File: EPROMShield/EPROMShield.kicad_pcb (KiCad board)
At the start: 2 copper layers, 101.6 x 53.3 mm, 79 parts, among them J1 Conn_02x16_Counter_Clockwise, P1 Digital, P10 CONN_01X01, P11 CONN_01X01, P12 CONN_01X01, P13 CONN_01X01, P2 Power, P3 Analog, P4 Analog, P5 PWM, P6 PWM, P7 Communication, P8 CONN_01X01, P9 CONN_01X01, Q1 BC847, Q2 BC847, Q3 BSS83P, Q4 BSS83P, Q5 BSS83P, Q6 BSS138, Q7 BC847, Q8 BC847, U1 MC34063AD, U2 LM317_TO-220, U3 74AHC1GU04

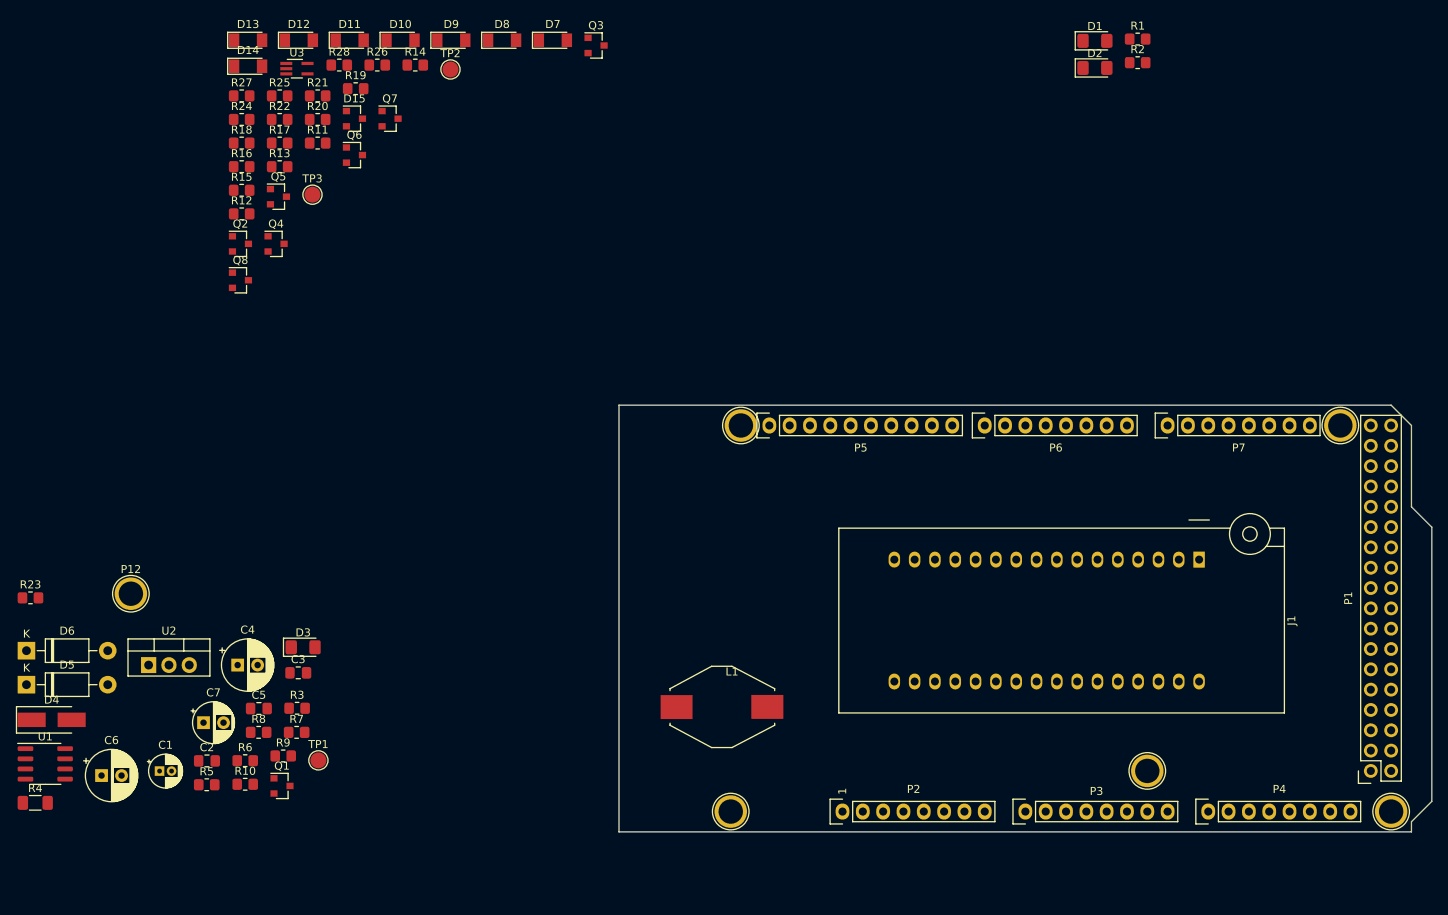
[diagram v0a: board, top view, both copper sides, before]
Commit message: First shot at component placement. Fixed VCC connection for Inverter
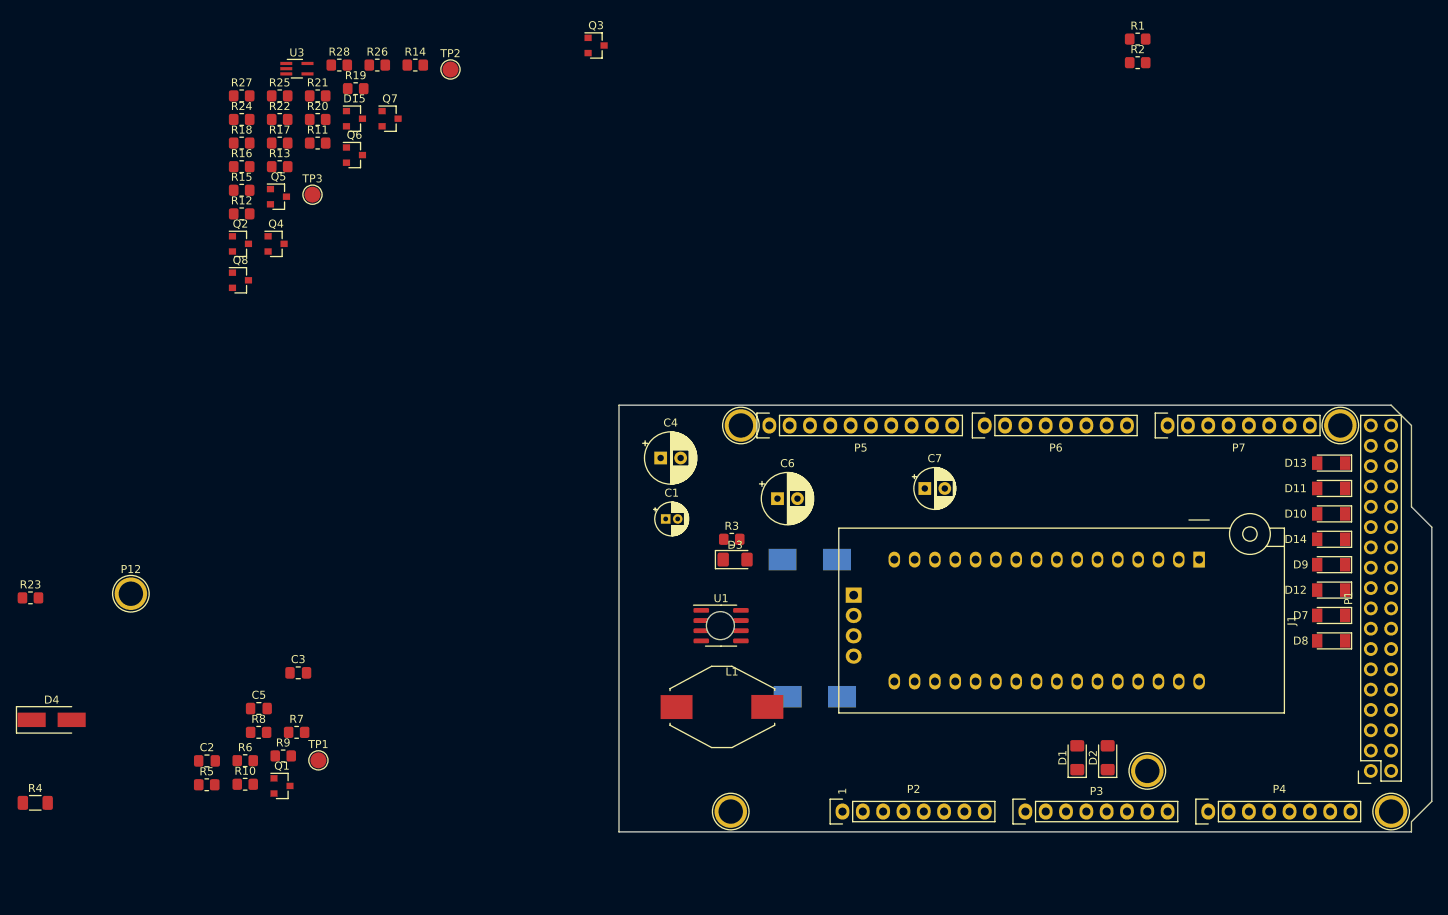
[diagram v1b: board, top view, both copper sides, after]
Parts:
- D5, D6: footprint Diode_THT:D_DO-41_SOD81_P10.16mm_Horizontal -> Diode_SMD:D_MELF_Handsoldering; moved to B.Cu
- U2: footprint Package_TO_SOT_THT:TO-220-3_Vertical -> Package_TO_SOT_THT:TO-220-4_Horizontal_TabDown; moved to B.Cu
- moved D14 147.7 mm to (192.4, 85.1), turned to 180 degrees
- moved D12 146.2 mm to (192.4, 91.4), turned to 180 degrees
- moved D13 145.3 mm to (192.4, 75.6), turned to 180 degrees
- moved D11 134.9 mm to (192.4, 78.7), turned to 180 degrees
- moved D10 130.5 mm to (192.4, 81.9), turned to 180 degrees
- moved D9 128.0 mm to (192.4, 88.3), turned to 180 degrees
- moved D8 128.0 mm to (192.4, 97.8), turned to 180 degrees
- moved D7 121.0 mm to (192.4, 94.6), turned to 180 degrees
- moved D6 98.6 mm to (127.2, 87.6)
- moved D5 98.6 mm to (127.9, 104.8)
- moved C7 94.8 mm to (141.6, 78.7)
- moved C6 91.3 mm to (123.2, 80.0)
- moved D1 89.6 mm to (160.7, 112.4), turned to 90 degrees
- moved U2 88.6 mm to (132.7, 92.1), turned to 270 degrees
- moved D2 86.2 mm to (164.5, 112.4), turned to 90 degrees
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
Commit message: First Version routing is done
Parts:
- C5, Q1, R10, R11, R12, R13, R14, R15, R16, R17, R18, R8, R9: moved to B.Cu
- D5, D6: footprint Diode_SMD:D_MELF_Handsoldering -> Diode_SMD:D_MELF
- U2: footprint Package_TO_SOT_THT:TO-220-4_Horizontal_TabDown -> Package_TO_SOT_THT:TO-220F-3_Horizontal_TabDown
- moved R24 153.8 mm to (186.7, 114.0), turned to 180 degrees
- moved U3 152.5 mm to (191.3, 109.0), turned to 180 degrees
- moved P12 151.8 mm to (189.9, 127.6)
- moved R22 146.7 mm to (185.7, 110.0), turned to 270 degrees
- moved R16 146.4 mm to (191.1, 95.2)
- moved R12 145.6 mm to (191.1, 99.2)
- moved R18 144.6 mm to (191.1, 87.6)
- moved R27 143.0 mm to (172.7, 112.5), turned to 270 degrees
- moved R11 142.3 mm to (191.1, 102.9)
- moved TP2 140.7 mm to (191.5, 115.1)
- moved R13 140.5 mm to (191.1, 91.4)
- moved R15 140.3 mm to (191.1, 80.0)
- moved C2 139.6 mm to (191.5, 112.3)
- moved Q4 136.7 mm to (181.4, 112.0), turned to 90 degrees
- moved R17 136.4 mm to (191.1, 76.2)
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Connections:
- C2 pad 1: GND -> VCC
- C7 pad 1: GND -> VCC
- D15 pad 1: GND -> VCC
- D5 pad 2: GND -> VCC
- D6 pad 1: GND -> VCC
- J1 pad 13: /37 -> /PGMSocket/Q0
- J1 pad 14: /36 -> /PGMSocket/Q1
- J1 pad 15: /35 -> /PGMSocket/Q2
- J1 pad 17: /34 -> /PGMSocket/Q3
- J1 pad 18: /33 -> /PGMSocket/Q4
- J1 pad 19: /32 -> /PGMSocket/Q5
- J1 pad 20: /31 -> /PGMSocket/Q6
- J1 pad 21: /30 -> /PGMSocket/Q7
- J1 pad 32: GND -> VCC
- J1 pad 7: /26 -> /27
- P1 pad 30: /26 -> /27
- Q4 pad 2: GND -> VCC
- R10 pad 1: GND -> VCC
- R11 pad 1: /37 -> /PGMSocket/Q0
- R12 pad 1: /36 -> /PGMSocket/Q1
- R13 pad 1: /35 -> /PGMSocket/Q2
- R14 pad 1: /34 -> /PGMSocket/Q3
- R15 pad 1: /33 -> /PGMSocket/Q4
- R16 pad 1: /32 -> /PGMSocket/Q5
- R17 pad 1: /31 -> /PGMSocket/Q6
- R18 pad 1: /30 -> /PGMSocket/Q7
- R24 pad 1: GND -> VCC
- TP1 pad 1: GND -> VCC
- U2 pad 2: GND -> VCC
- U3 pad 5: GND -> VCC
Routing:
- net GND: track 0.00 -> 165.2 mm, vias 0 -> 16
- net +5V: track 0.00 -> 137.9 mm
- net VPP: track 0.00 -> 126.4 mm, vias 0 -> 5
- net VCC: track 0.00 -> 121.0 mm, vias 0 -> 3
- net /PGMSocket/Q3: track 0.00 -> 88.3 mm, vias 0 -> 5
- net /PGMSocket/Q4: track 0.00 -> 84.7 mm, vias 0 -> 3
- net /PGMSocket/Q1: track 0.00 -> 76.6 mm, vias 0 -> 3
- net /PGMSocket/Q6: track 0.00 -> 73.3 mm, vias 0 -> 1
- net /PGMSocket/Q0: track 0.00 -> 66.8 mm, vias 0 -> 2
- net /23: track 0.00 -> 63.1 mm
- net /22: track 0.00 -> 61.8 mm
- net /25: track 0.00 -> 59.1 mm, vias 0 -> 1
- net /24: track 0.00 -> 57.6 mm
- net /PGMSocket/Q7: track 0.00 -> 55.5 mm, vias 0 -> 2
- net /38: track 0.00 -> 55.1 mm, vias 0 -> 1
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- added copper zone on B.Cu, net GND
- added copper zone on F.Cu, net GND
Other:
- net class Switcher added: clearance 0.2, trace_width 0.75, via_dia 0.6, via_drill 0.4

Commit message: Routing update
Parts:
- removed P12, P9: CONN_01X01, Socket_Arduino_Mega:Arduino_1pin
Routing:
- net /39: track 32.4 -> 35.7 mm
